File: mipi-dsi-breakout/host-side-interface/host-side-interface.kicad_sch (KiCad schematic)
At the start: 17 parts, among them J2 Conn_01x03_Pin, J3 Conn_01x03_Pin, J4 Conn_01x03_Pin

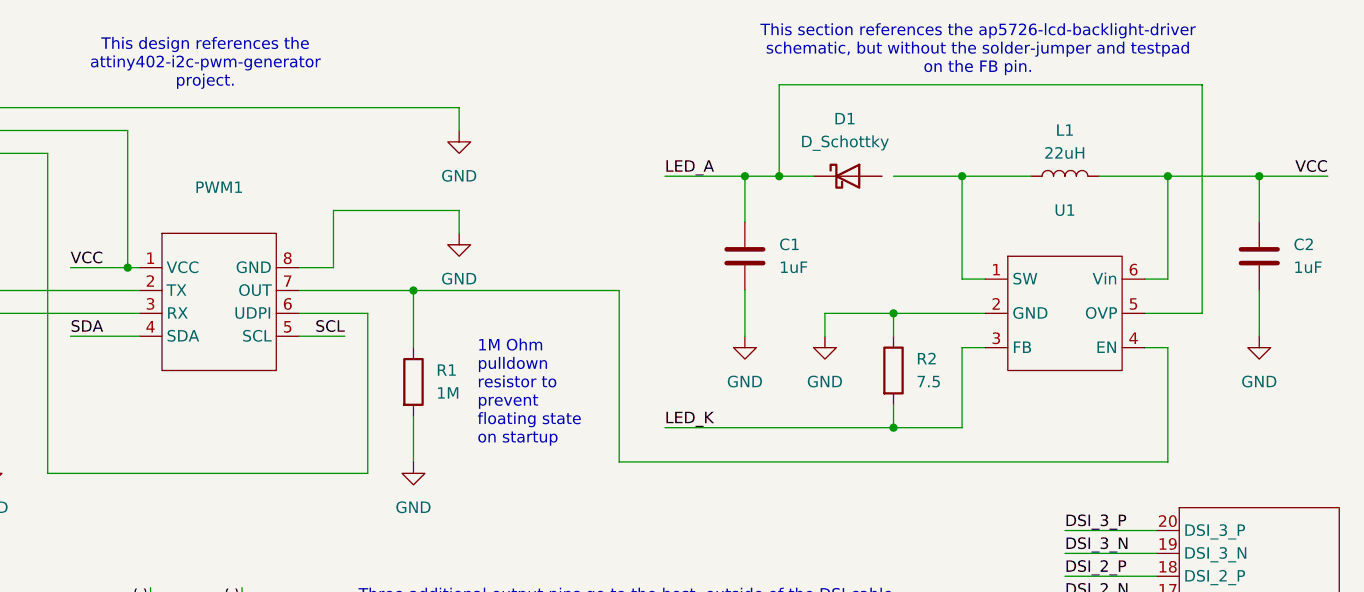
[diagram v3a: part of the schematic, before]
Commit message: Change PWM symbol to attiny402.
Be more specific about which part it should be.

Also fix ERC issue with AP5726 on the host-side-interface with
unconnected schottky diode.
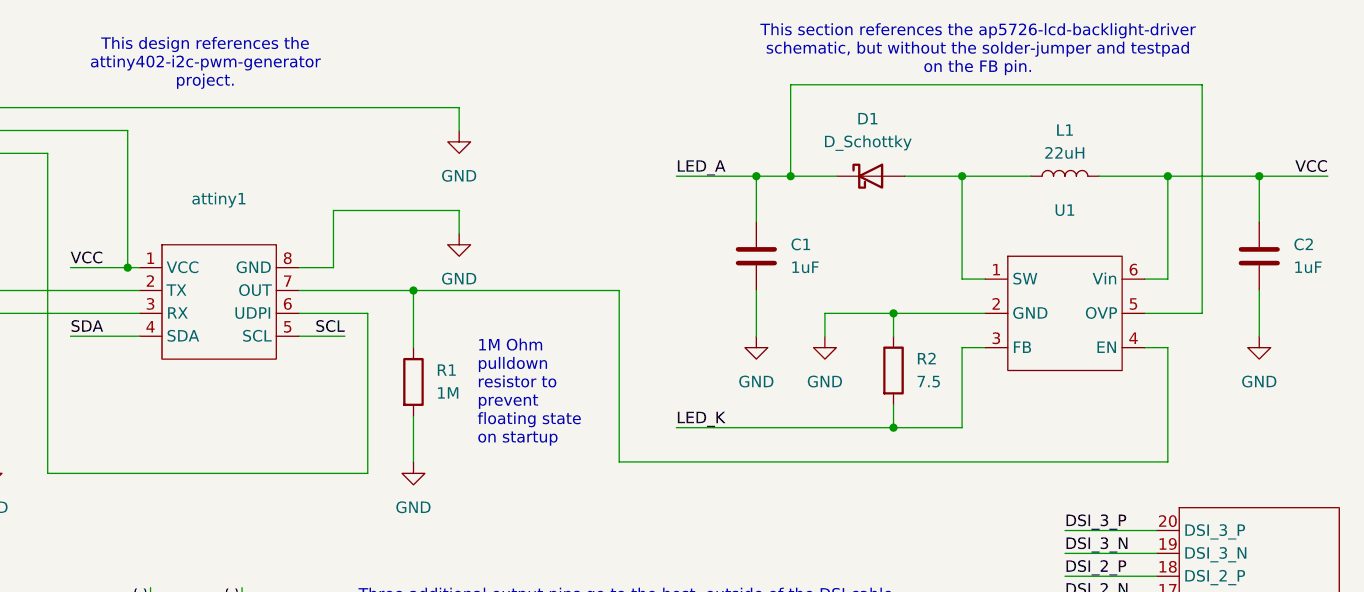
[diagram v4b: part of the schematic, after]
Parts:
- removed PWM1: ~, symbol project:pwm_generator
- added attiny1: ~, symbol project:attiny402
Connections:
- net GND: now also attiny1.8 (GND)
- net SCL: now also attiny1.5 (SCL)
- net SDA: now also attiny1.4 (SDA)
- net VCC: now also attiny1.1 (VCC)
- net at J3.3 (Pin_3): now also attiny1.6 (UDPI)
- net at L1.1, U1.1 (SW): now also D1.2 (A)
- net at R1.1, U1.4 (EN): now also attiny1.7 (OUT)
- net at J4.1 (Pin_1): now also attiny1.2 (TX)
- net at J4.2 (Pin_2): now also attiny1.3 (RX)
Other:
- moved on the sheet: C1, D1
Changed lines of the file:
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@@
 	)
 	(junction
-		(at 176.53 60.96)
+		(at 218.44 148.59)
 		(diameter 0)
 		(color 0 0 0 0)
 	)
 	(junction
-		(at 218.44 148.59)
+		(at 190.5 146.05)
 		(diameter 0)
 		(color 0 0 0 0)
 	)
 	(junction
-		(at 190.5 146.05)
+		(at 181.61 60.96)
 		(diameter 0)
 		(color 0 0 0 0)
@@
 	)
 	(junction
-		(at 180.34 60.96)
+		(at 177.8 60.96)
 		(diameter 0)
 		(color 0 0 0 0)
@@
 	(wire
 		(pts
+			(xy 181.61 60.96) (xy 186.69 60.96)
+		)
+		(stroke
+			(width 0)
+			(type default)
+		)
+	)
+	(wire
+		(pts
 			(xy 189.23 125.73) (xy 138.43 125.73)
 		)
@@
 	(wire
 		(pts
-			(xy 227.33 50.8) (xy 180.34 50.8)
+			(xy 227.33 50.8) (xy 181.61 50.8)
 		)
 		(stroke
@@
 	(wire
 		(pts
-			(xy 180.34 50.8) (xy 180.34 60.96)
+			(xy 181.61 50.8) (xy 181.61 60.96)
 		)
 		(stroke
@@
 	(wire
 		(pts
-			(xy 167.64 60.96) (xy 176.53 60.96)
+			(xy 168.91 60.96) (xy 177.8 60.96)
 		)
 		(stroke
@@
 	(wire
 		(pts
-			(xy 180.34 60.96) (xy 184.15 60.96)
+			(xy 86.36 125.73) (xy 86.36 137.16)
 		)
 		(stroke
@@
 	(wire
 		(pts
-			(xy 86.36 125.73) (xy 86.36 137.16)
+			(xy 116.84 123.19) (xy 120.65 123.19)
 		)
 		(stroke
@@
 	(wire
 		(pts
-			(xy 116.84 123.19) (xy 120.65 123.19)
+			(xy 109.22 73.66) (xy 90.17 73.66)
 		)
 		(stroke
@@
 	(wire
 		(pts
-			(xy 109.22 73.66) (xy 90.17 73.66)
+			(xy 220.98 80.01) (xy 223.52 80.01)
 		)
 		(stroke
@@
 	(wire
 		(pts
-			(xy 220.98 80.01) (xy 223.52 80.01)
+			(xy 177.8 60.96) (xy 181.61 60.96)
 		)
 		(stroke
@@
 	(wire
 		(pts
-			(xy 176.53 60.96) (xy 180.34 60.96)
-		)
-		(stroke
-			(width 0)
-			(type default)
-		)
-	)
-	(wire
-		(pts
-			(xy 176.53 73.66) (xy 176.53 78.74)
+			(xy 177.8 73.66) (xy 177.8 78.74)
 		)
 		(stroke
@@
 	(wire
 		(pts
-			(xy 167.64 88.9) (xy 193.04 88.9)
+			(xy 168.91 88.9) (xy 193.04 88.9)
 		)
 		(stroke
@@
 	(wire
 		(pts
-			(xy 193.04 60.96) (xy 200.66 60.96)
-		)
-		(stroke
-			(width 0)
-			(type default)
-		)
-	)
-	(wire
-		(pts
 			(xy 200.66 60.96) (xy 200.66 72.39)
 		)
@@
 	(wire
 		(pts
+			(xy 194.31 60.96) (xy 200.66 60.96)
+		)
+		(stroke
+			(width 0)
+			(type default)
+		)
+	)
+	(wire
+		(pts
 			(xy 92.71 83.82) (xy 85.09 83.82)
 		)
@@
 	(wire
 		(pts
-			(xy 176.53 60.96) (xy 176.53 66.04)
+			(xy 177.8 60.96) (xy 177.8 66.04)
 		)
 		(stroke
@@
 	)
 	(label "LED_A"
-		(at 167.64 60.96 0)
+		(at 168.91 60.96 0)
 		(effects
 			(font
@@
 	)
 	(label "LED_K"
-		(at 167.64 88.9 0)
+		(at 168.91 88.9 0)
 		(effects
 			(font
@@
 	(symbol
 		(lib_id "Device:C")
-		(at 176.53 69.85 0)
+		(at 177.8 69.85 0)
 		(unit 1)
 		(exclude_from_sim no)
@@
 		(fields_autoplaced yes)
 		(property "Reference" "C1"
-			(at 180.34 68.5799 0)
+			(at 181.61 68.5799 0)
 			(effects
 				(font
@@
 		)
 		(property "Value" "1uF"
-			(at 180.34 71.1199 0)
+			(at 181.61 71.1199 0)
 			(effects
 				(font
@@
 		)
 		(property "Footprint" ""
-			(at 177.4952 73.66 0)
+			(at 178.7652 73.66 0)
 			(effects
 				(font
@@
 		)
 		(property "Datasheet" "~"
-			(at 176.53 69.85 0)
+			(at 177.8 69.85 0)
 			(effects
 				(font
@@
 		)
 		(property "Description" "Unpolarized capacitor"
-			(at 176.53 69.85 0)
+			(at 177.8 69.85 0)
 			(effects
 				(font
@@
 	)
 	(symbol
-		(lib_id "Device:L")
-		(at 212.09 60.96 90)
+		(lib_id "project:attiny402")
+		(at 118.11 74.93 0)
 		(unit 1)
 		(exclude_from_sim no)
@@
 		(dnp no)
 		(fields_autoplaced yes)
-		(property "Reference" "L1"
-			(at 212.09 55.88 90)
+		(property "Reference" "attiny1"
+			(at 118.11 63.5 0)
 			(effects
 				(font
@@
 			)
 		)
-		(property "Value" "22uH"
-			(at 212.09 58.42 90)
+		(property "Value" "~"
+			(at 118.11 66.04 0)
 			(effects
 				(font
@@
 		)
 		(property "Footprint" ""
-			(at 212.09 60.96 0)
+			(at 118.11 74.93 0)
 			(effects
 				(font
@@
 			)
 		)
-		(property "Datasheet" "~"
-			(at 212.09 60.96 0)
+		(property "Datasheet" ""
+			(at 118.11 74.93 0)
 			(effects
 				(font
@@
 			)
 		)
-		(property "Description" "Inductor"
-			(at 212.09 60.96 0)
+		(property "Description" ""
+			(at 118.11 74.93 0)
 			(effects
 				(font
@@
 			)
 		)
-		(pin "1"
+		(pin "5"
 		)
 		(pin "2"
 		)
+		(pin "8"
+		)
+		(pin "7"
+		)
+		(pin "4"
+		)
+		(pin "6"
+		)
+		(pin "3"
+		)
+		(pin "1"
+		)
 		(instances
 			(project ""
 				(path "/f2077993-b821-4408-bc59-2d0bd14a1026"
-					(reference "L1")
+					(reference "attiny1")
 					(unit 1)
 				)
@@
 	)
 	(symbol
-		(lib_id "project:pwm_generator")
-		(at 118.11 74.93 0)
+		(lib_id "Device:L")
+		(at 212.09 60.96 90)
 		(unit 1)
 		(exclude_from_sim no)
@@
 		(dnp no)
 		(fields_autoplaced yes)
-		(property "Reference" "PWM1"
-			(at 118.11 62.23 0)
+		(property "Reference" "L1"
+			(at 212.09 55.88 90)
 			(effects
 				(font
@@
 			)
 		)
-		(property "Value" "~"
-			(at 118.11 64.77 0)
+		(property "Value" "22uH"
+			(at 212.09 58.42 90)
 			(effects
 				(font
@@
 		)
 		(property "Footprint" ""
-			(at 118.11 74.93 0)
+			(at 212.09 60.96 0)
 			(effects
 				(font
@@
 			)
 		)
-		(property "Datasheet" ""
-			(at 118.11 74.93 0)
+		(property "Datasheet" "~"
+			(at 212.09 60.96 0)
 			(effects
 				(font
@@
 			)
 		)
-		(property "Description" ""
-			(at 118.11 74.93 0)
+		(property "Description" "Inductor"
+			(at 212.09 60.96 0)
 			(effects
 				(font
@@
 		(pin "1"
 		)
-		(pin "7"
-		)
-		(pin "5"
-		)
 		(pin "2"
 		)
-		(pin "6"
-		)
-		(pin "3"
-		)
-		(pin "8"
-		)
-		(pin "4"
-		)
 		(instances
 			(project ""
 				(path "/f2077993-b821-4408-bc59-2d0bd14a1026"
-					(reference "PWM1")
+					(reference "L1")
 					(unit 1)
 				)
@@
 	(symbol
 		(lib_id "power:GND")
-		(at 176.53 78.74 0)
+		(at 177.8 78.74 0)
 		(unit 1)
 		(exclude_from_sim no)
@@
 		(fields_autoplaced yes)
 		(property "Reference" "#PWR04"
-			(at 176.53 85.09 0)
+			(at 177.8 85.09 0)
 			(effects
 				(font
@@
 		)
 		(property "Value" "GND"
-			(at 176.53 83.82 0)
+			(at 177.8 83.82 0)
 			(effects
 				(font
@@
 		)
 		(property "Footprint" ""
-			(at 176.53 78.74 0)
+			(at 177.8 78.74 0)
 			(effects
 				(font
@@
 		)
 		(property "Datasheet" ""
-			(at 176.53 78.74 0)
+			(at 177.8 78.74 0)
 			(effects
 				(font
@@
 		)
 		(property "Description" "Power symbol creates a global label with name \"GND\" , ground"
-			(at 176.53 78.74 0)
+			(at 177.8 78.74 0)
 			(effects
 				(font
@@
 	(symbol
 		(lib_id "Device:D_Schottky")
-		(at 187.96 60.96 0)
+		(at 190.5 60.96 0)
 		(unit 1)
 		(exclude_from_sim no)
@@
 		(fields_autoplaced yes)
 		(property "Reference" "D1"
-			(at 187.6425 54.61 0)
+			(at 190.1825 54.61 0)
 			(effects
 				(font
@@
 		)
 		(property "Value" "D_Schottky"
-			(at 187.6425 57.15 0)
+			(at 190.1825 57.15 0)
 			(effects
 				(font
@@
 		)
 		(property "Footprint" ""
-			(at 187.96 60.96 0)
+			(at 190.5 60.96 0)
 			(effects
 				(font
@@
 		)
 		(property "Datasheet" "~"
-			(at 187.96 60.96 0)
+			(at 190.5 60.96 0)
 			(effects
 				(font
@@
 		)
 		(property "Description" "Schottky diode"
-			(at 187.96 60.96 0)
+			(at 190.5 60.96 0)
 			(effects
 				(font
